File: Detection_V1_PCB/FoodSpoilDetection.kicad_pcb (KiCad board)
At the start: 2 copper layers, 7 parts, among them J1 Conn_01x07_Pin, J2 Conn_01x07_Pin, J3 Conn_01x03_Pin, J4 Conn_01x03_Pin, J5 Conn_01x03_Pin, J6 Conn_01x10_Pin, Q1 Q_NMOS_GSD

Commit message: pcb edits
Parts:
- added J7: Conn_01x04_Pin, Connector_PinHeader_2.54mm:PinHeader_1x04_P2.54mm_Vertical, F.Cu at (218.2, 47.0)
- added Q2: Q_NMOS_GSD, BSS138:SOT-23_3L_ONS, F.Cu at (124.0, 84.0)
- added R1: 10k, Resistor_SMD:R_0603_1608Metric_Pad0.98x0.95mm_HandSolder, F.Cu at (131.5, 88.5)
- added R2: 10k, Resistor_SMD:R_0603_1608Metric_Pad0.98x0.95mm_HandSolder, F.Cu at (124.0, 88.5)
- added R3: 10k, Resistor_SMD:R_0603_1608Metric_Pad0.98x0.95mm_HandSolder, F.Cu at (124.1, 79.0)
- added R4: 10k, Resistor_SMD:R_0603_1608Metric_Pad0.98x0.95mm_HandSolder, F.Cu at (131.5, 79.0)
- moved J2 57.4 mm to (116.4, 30.5), turned to 90 degrees
- moved J1 45.7 mm to (131.6, 40.5), turned to -90 degrees
- moved J5 43.1 mm to (190.4, 47.0), turned to 90 degrees
- moved J4 38.8 mm to (174.5, 47.0), turned to 90 degrees
- moved J6 25.6 mm to (164.4, 67.5), turned to -90 degrees
- moved J3 21.7 mm to (158.4, 47.5), turned to 90 degrees
- moved Q1 8.23 mm to (131.5, 84.0), turned to 180 degrees
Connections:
- J3 pad 3: /Vout -> /5V-A0
- J4 pad 3: /Vout -> /5V-A1
- J5 pad 3: /Vout -> /5V-A2
- Q1 pad 1: unconnected-(Q1-G-Pad1) -> /3V3
- Q1 pad 2: unconnected-(Q1-S-Pad2) -> /SCL-3V
- Q1 pad 3: unconnected-(Q1-D-Pad3) -> /SCL-5V
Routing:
- net /5V: track 0.00 -> 475.4 mm
- net /GND: track 0.00 -> 358.3 mm, vias 0 -> 5
- net /SDA-5V: track 0.00 -> 137.6 mm
- net /SCL-5V: track 0.00 -> 117.7 mm
- net /3V3: track 0.00 -> 114.8 mm
- net /SDA-3V: track 0.00 -> 43.9 mm
- net /SCL-3V: track 0.00 -> 43.1 mm
- net /5V-A2: track 0.00 -> 42.1 mm
- net /5V-A1: track 0.00 -> 28.9 mm
- net /5V-A0: track 0.00 -> 22.8 mm

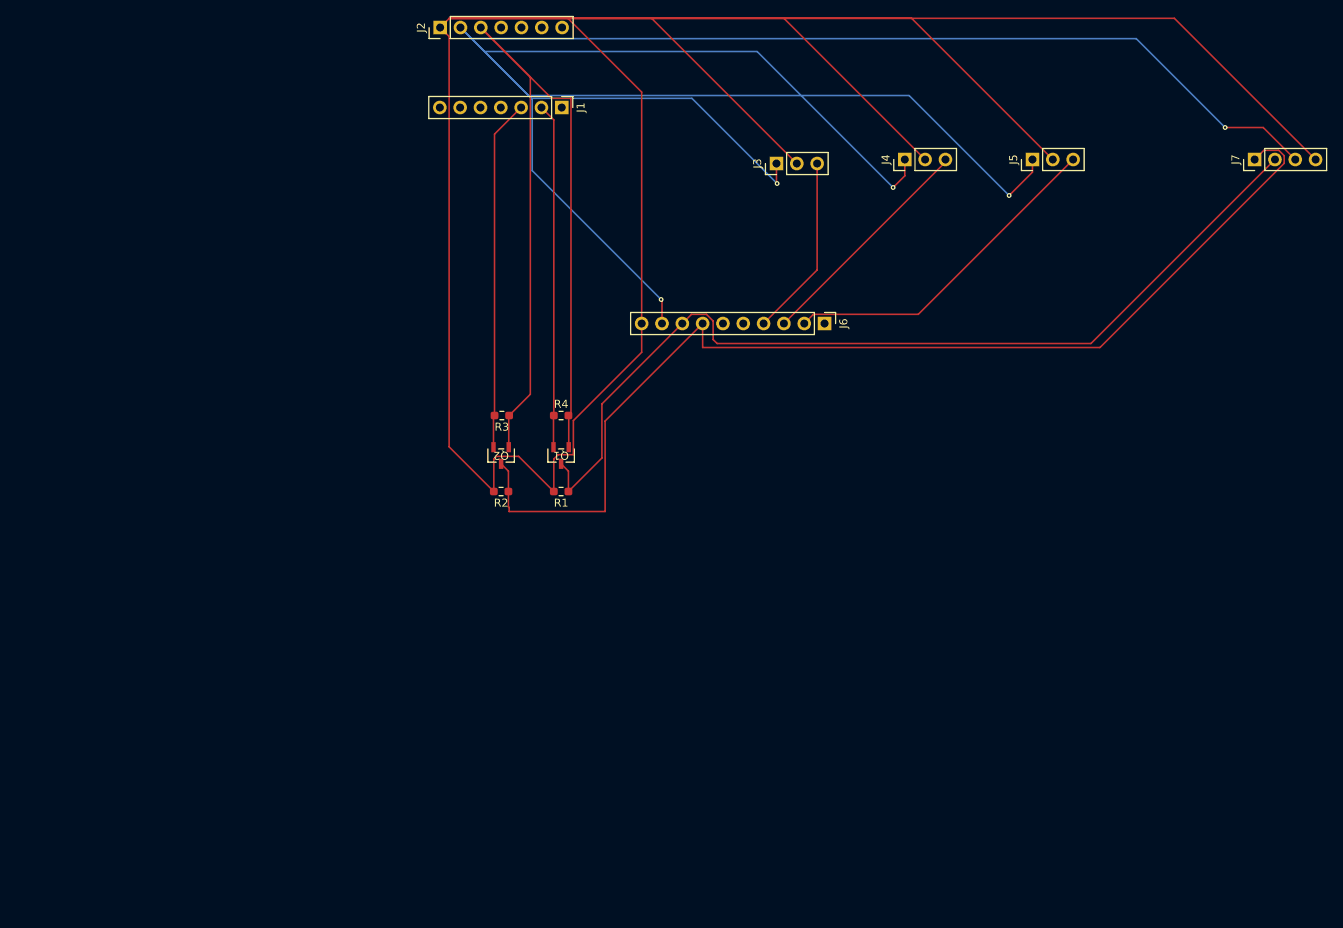
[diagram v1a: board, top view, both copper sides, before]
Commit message: changes to PCB -- Added LEDs and rearranged Layout
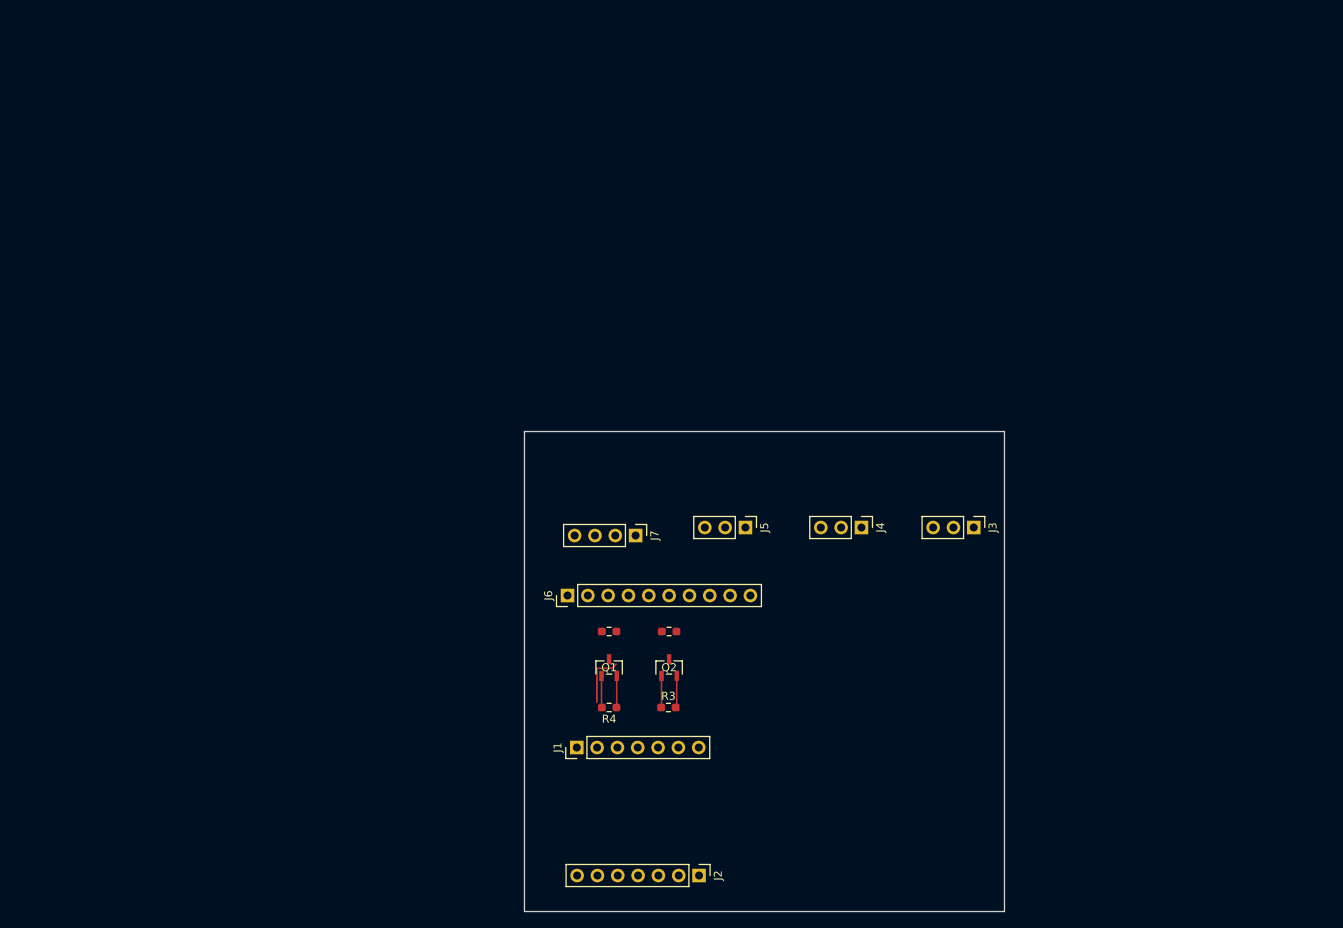
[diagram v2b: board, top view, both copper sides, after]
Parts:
- moved J2 110.8 mm to (148.7, 136.5), turned to -90 degrees
- moved J7 90.5 mm to (140.8, 94.0), turned to -90 degrees
- moved J1 80.0 mm to (133.5, 120.5), turned to 90 degrees
- moved J5 58.3 mm to (154.5, 93.0), turned to -90 degrees
- moved J3 51.8 mm to (183.1, 93.0), turned to -90 degrees
- moved J6 46.8 mm to (132.3, 101.5), turned to 90 degrees
- moved J4 46.3 mm to (169.0, 93.0), turned to -90 degrees
- moved R3 42.0 mm to (144.9, 115.5), turned to 0 degrees
- moved R4 37.0 mm to (137.5, 115.5), turned to 180 degrees
- moved Q2 33.8 mm to (145.0, 110.5), turned to 0 degrees
- moved R2 27.3 mm to (145.0, 106.0), turned to 0 degrees
- moved Q1 27.2 mm to (137.5, 110.5), turned to 0 degrees
- moved R1 18.5 mm to (137.5, 106.0), turned to 0 degrees
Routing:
- net /5V: track 475.4 -> 6.93 mm
- net /GND: track 358.3 -> 0.00 mm, vias 5 -> 0
- net /SDA-5V: track 137.6 -> 0.00 mm
- net /SCL-5V: track 117.7 -> 0.00 mm
- net /3V3: track 114.8 -> 8.40 mm
- net /5V-A2: track 42.1 -> 0.00 mm
- net /SDA-3V: track 43.9 -> 4.01 mm
- net /SCL-3V: track 43.1 -> 3.98 mm
- net /5V-A1: track 28.9 -> 0.00 mm
- net /5V-A0: track 22.8 -> 0.00 mm
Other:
- board outline added: 60 x 60 mm

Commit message: pcb changes
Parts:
- removed R4: 10k, Resistor_SMD:R_0603_1608Metric_Pad0.98x0.95mm_HandSolder
- added D1: LED, LED_SMD:LED_0603_1608Metric_Pad1.05x0.95mm_HandSolder, F.Cu at (87.4, 110.3)
- added D2: LED, LED_SMD:LED_0603_1608Metric_Pad1.05x0.95mm_HandSolder, F.Cu at (87.4, 112.9)
- added D3: LED, LED_SMD:LED_0603_1608Metric_Pad1.05x0.95mm_HandSolder, F.Cu at (87.4, 115.5)
- added D4: LED, LED_SMD:LED_0603_1608Metric_Pad1.05x0.95mm_HandSolder, F.Cu at (87.4, 118.1)
- added D5: LED, LED_SMD:LED_0603_1608Metric_Pad1.05x0.95mm_HandSolder, F.Cu at (87.4, 120.7)
- added D6: LED, LED_SMD:LED_0603_1608Metric_Pad1.05x0.95mm_HandSolder, F.Cu at (87.4, 123.2)
- added D7: LED, LED_SMD:LED_0603_1608Metric_Pad1.05x0.95mm_HandSolder, F.Cu at (87.4, 125.8)
- added D8: LED, LED_SMD:LED_0603_1608Metric_Pad1.05x0.95mm_HandSolder, F.Cu at (87.4, 128.4)
- added Q3: AO3401A, Package_TO_SOT_SMD:SOT-23, F.Cu at (78.1, 90.4)
- Q1: value Q_NMOS_GSD -> AO3400A; footprint BSS138:SOT-23_3L_ONS -> Package_TO_SOT_SMD:SOT-23
- Q2: value Q_NMOS_GSD -> AO3401A; footprint BSS138:SOT-23_3L_ONS -> Package_TO_SOT_SMD:SOT-23
- R1: value 10k -> 10ohm
- R2, R3: value 10k -> 100k
- moved J2 69.2 mm to (80.0, 128.4)
- moved J3 67.3 mm to (116.1, 86.9)
- moved J7 67.3 mm to (73.8, 87.9)
- moved J4 67.3 mm to (102.0, 86.9)
- moved J5 67.3 mm to (87.5, 86.9)
- moved J1 66.8 mm to (68.8, 103.9)
- moved R3 66.6 mm to (83.0, 90.9)
- moved Q2 56.9 mm to (92.4, 88.8)
- moved R2 50.0 mm to (97.0, 91.9)
- moved Q1 45.8 mm to (93.1, 121.4)
- moved R1 44.3 mm to (93.6, 111.9)
- moved J6 26.4 mm to (111.0, 117.0), turned to 180 degrees
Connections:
- J3 pad 2: /5V -> Net-(J3-Pin_2)
- J3 pad 3: /5V-A0 -> /A1
- J4 pad 2: /5V -> Net-(J3-Pin_2)
- J4 pad 3: /5V-A1 -> (no net)
- J5 pad 2: /5V -> Net-(J3-Pin_2)
- J5 pad 3: /5V-A2 -> /A3
- J6 pad 1: /5V-A3 -> /A3
- J6 pad 10: /5V -> /3V3
- J6 pad 2: /5V-A2 -> (no net)
- J6 pad 3: /5V-A1 -> /A1
- J6 pad 4: /5V-A0 -> /A0
- J6 pad 7: /SDA-5V -> /SDA-3V
- J6 pad 8: /SCL-5V -> /SCL-3V
- J7 pad 1: /SDA-5V -> /SDA-3V
- J7 pad 2: /SCL-5V -> /SCL-3V
- J7 pad 4: /5V -> Net-(J7-Pin_4)
- Q1 pad 1: /3V3 -> /D7
- Q1 pad 2: /SCL-3V -> /GND
- Q1 pad 3: /SCL-5V -> Net-(D1-K)
- Q2 pad 1: /3V3 -> /D9
- Q2 pad 2: /SDA-3V -> /GND
- Q2 pad 3: /SDA-5V -> Net-(J3-Pin_2)
- R1 pad 1: /SCL-5V -> /3V3
- R1 pad 2: /5V -> Net-(D1-A)
- R2 pad 1: /SDA-5V -> /3V3
- R2 pad 2: /5V -> /D9
- R3 pad 2: /SDA-3V -> /D10
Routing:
- net Net-(D1-A): track 0.00 -> 31.1 mm
- net /3V3: track 8.40 -> 0.00 mm
- net /5V: track 6.93 -> 0.00 mm
- net /SDA-3V: track 4.01 -> 0.00 mm
- net /SCL-3V: track 3.98 -> 0.00 mm

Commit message: updated schematic (almost finalized)
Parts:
- removed J1, J2: Conn_01x07_Pin, Connector_PinHeader_2.54mm:PinHeader_1x07_P2.54mm_Vertical
- added J9: Conn_01x10_Socket, Connector_PinSocket_2.54mm:PinSocket_1x10_P2.54mm_Vertical, F.Cu at (167.3, 134.6)
- added R10: 100K, Resistor_SMD:R_0603_1608Metric_Pad0.98x0.95mm_HandSolder, F.Cu at (103.6, 114.8)
- added R11: 100K, Resistor_SMD:R_0603_1608Metric_Pad0.98x0.95mm_HandSolder, F.Cu at (103.6, 117.3)
- added R4: 1K, Resistor_SMD:R_0603_1608Metric_Pad0.98x0.95mm_HandSolder, F.Cu at (99.2, 114.8)
- added R5: 1K, Resistor_SMD:R_0603_1608Metric_Pad0.98x0.95mm_HandSolder, F.Cu at (99.2, 117.3)
- added R6: 1K, Resistor_SMD:R_0603_1608Metric_Pad0.98x0.95mm_HandSolder, F.Cu at (99.2, 119.9)
- added R7: 1K, Resistor_SMD:R_0603_1608Metric_Pad0.98x0.95mm_HandSolder, F.Cu at (103.6, 107.3)
- added R8: 1K, Resistor_SMD:R_0603_1608Metric_Pad0.98x0.95mm_HandSolder, F.Cu at (103.6, 109.8)
- added R9: 100K, Resistor_SMD:R_0603_1608Metric_Pad0.98x0.95mm_HandSolder, F.Cu at (103.6, 112.3)
- added U1: XIAO-ESP32-S3-DIP, esp32s3:XIAO-ESP32-S3-DIP, F.Cu at (155.4, 107.4)
- D1, D2, D3, D4, D5, D6, D7, D8: footprint LED_SMD:LED_0603_1608Metric_Pad1.05x0.95mm_HandSolder -> LED_SMD:LED_0603_1608Metric
- J3, J4: value Conn_01x03_Pin -> Conn_01x03_Socket; footprint Connector_PinHeader_2.54mm:PinHeader_1x03_P2.54mm_Vertical -> Connector_PinSocket_2.54mm:PinSocket_1x03_P2.54mm_Vertical
- J5: value Conn_01x03_Pin -> Conn_01x04_Socket; footprint Connector_PinHeader_2.54mm:PinHeader_1x03_P2.54mm_Vertical -> Connector_PinSocket_2.54mm:PinSocket_1x04_P2.54mm_Vertical
- J6: value Conn_01x10_Pin -> Conn_01x03_Socket; footprint Connector_PinHeader_2.54mm:PinHeader_1x10_P2.54mm_Vertical -> Connector_PinSocket_2.54mm:PinSocket_1x03_P2.54mm_Vertical
- J7: value Conn_01x04_Pin -> Conn_01x06_Socket; footprint Connector_PinHeader_2.54mm:PinHeader_1x04_P2.54mm_Vertical -> Connector_PinSocket_2.54mm:PinSocket_1x06_P2.54mm_Vertical
- R1: value 10ohm -> 1K
- R2, R3: value 100k -> 1K
- moved D2 87.7 mm to (173.0, 94.0)
- moved D7 86.9 mm to (172.2, 107.2)
- moved D5 85.2 mm to (172.6, 119.6)
- moved D1 71.1 mm to (156.2, 92.6)
- moved D8 69.0 mm to (155.8, 119.8)
- moved Q3 68.4 mm to (130.1, 134.8)
- moved J7 62.2 mm to (135.8, 93.3), turned to 0 degrees
- moved J3 58.2 mm to (174.2, 83.4)
- moved D3 57.3 mm to (140.2, 93.2)
- moved J6 56.8 mm to (156.8, 83.4), turned to -90 degrees
- moved Q2 53.5 mm to (130.1, 126.8)
- moved D4 53.1 mm to (139.6, 108.6)
- moved D6 52.7 mm to (140.0, 120.0)
- moved J5 40.7 mm to (127.2, 96.0), turned to 0 degrees
- moved Q1 36.5 mm to (129.5, 118.4)
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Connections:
- D2 pad 2: Net-(D1-A) -> Net-(D2-A)
- D3 pad 2: Net-(D1-A) -> Net-(D3-A)
- D4 pad 2: Net-(D1-A) -> Net-(D4-A)
- D5 pad 2: Net-(D1-A) -> Net-(D5-A)
- D6 pad 2: Net-(D1-A) -> Net-(D6-A)
- D7 pad 2: Net-(D1-A) -> Net-(D7-A)
- D8 pad 2: Net-(D1-A) -> Net-(D8-A)
- J3 pad 1: /GND -> /A1
- J3 pad 3: /A1 -> GND
- J4 pad 1: /GND -> /A2
- J4 pad 3: (no net) -> GND
- J5 pad 1: /GND -> Net-(J5-Pin_1)
- J5 pad 2: Net-(J3-Pin_2) -> GND
- J5 pad 3: /A3 -> SCL
- J6 pad 2: (no net) -> Net-(J3-Pin_2)
- J6 pad 3: /A1 -> GND
- J7 pad 1: /SDA-3V -> unconnected-(J7-Pin_1-Pad1)
- J7 pad 2: /SCL-3V -> unconnected-(J7-Pin_2-Pad2)
- J7 pad 3: /GND -> unconnected-(J7-Pin_3-Pad3)
- J7 pad 4: Net-(J7-Pin_4) -> unconnected-(J7-Pin_4-Pad4)
- Q1 pad 1: /D7 -> Net-(Q1-G)
- Q1 pad 2: /GND -> GND
- Q2 pad 1: /D9 -> D1
- Q2 pad 2: /GND -> GND
- Q3 pad 1: /D10 -> D0
- Q3 pad 2: /GND -> GND
- Q3 pad 3: Net-(J7-Pin_4) -> Net-(J5-Pin_1)
- R1 pad 1: /3V3 -> Net-(D2-A)
- R1 pad 2: Net-(D1-A) -> 3v3
- R2 pad 1: /3V3 -> Net-(D1-A)
- R2 pad 2: /D9 -> 3v3
- R3 pad 1: /3V3 -> Net-(D3-A)
- R3 pad 2: /D10 -> 3v3
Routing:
- net Net-(D1-A): track 31.1 -> 0.00 mm

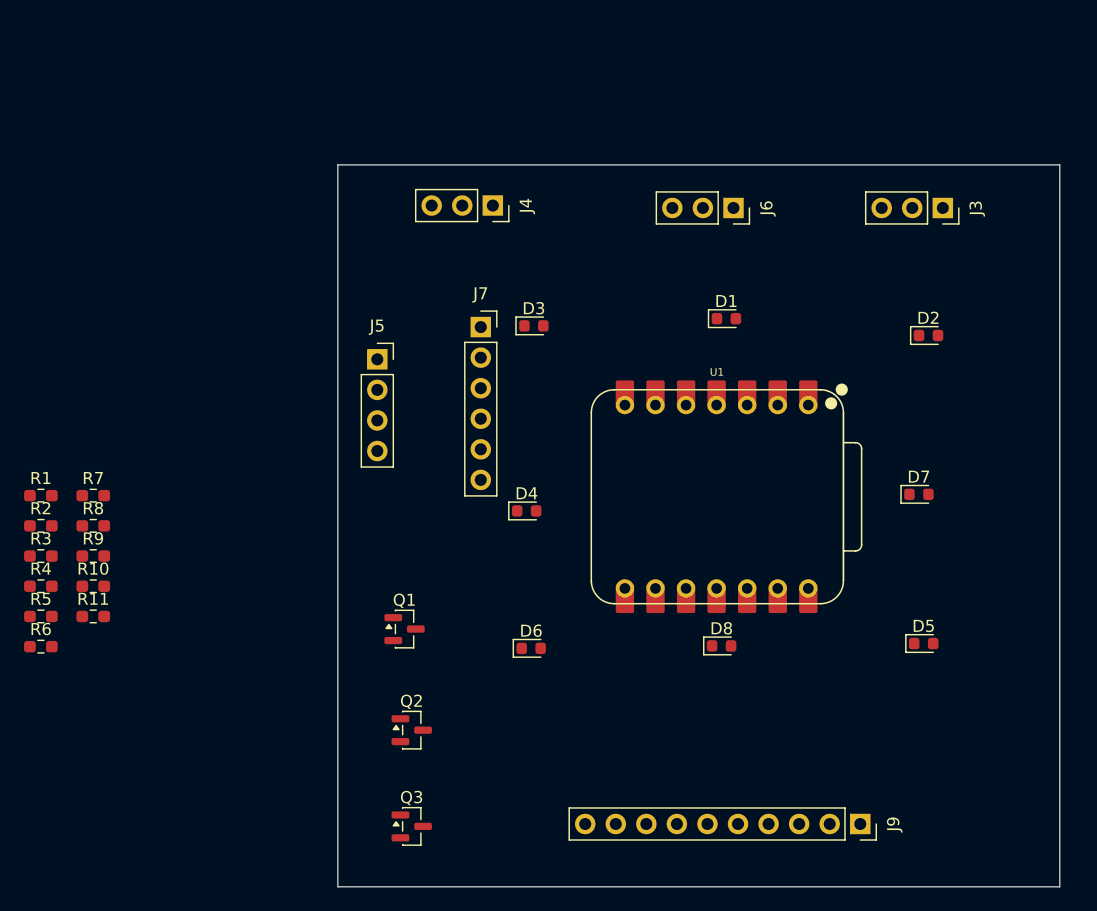
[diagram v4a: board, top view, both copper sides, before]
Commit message: added mounting holes
Need to align mounting holes and fiduciaries
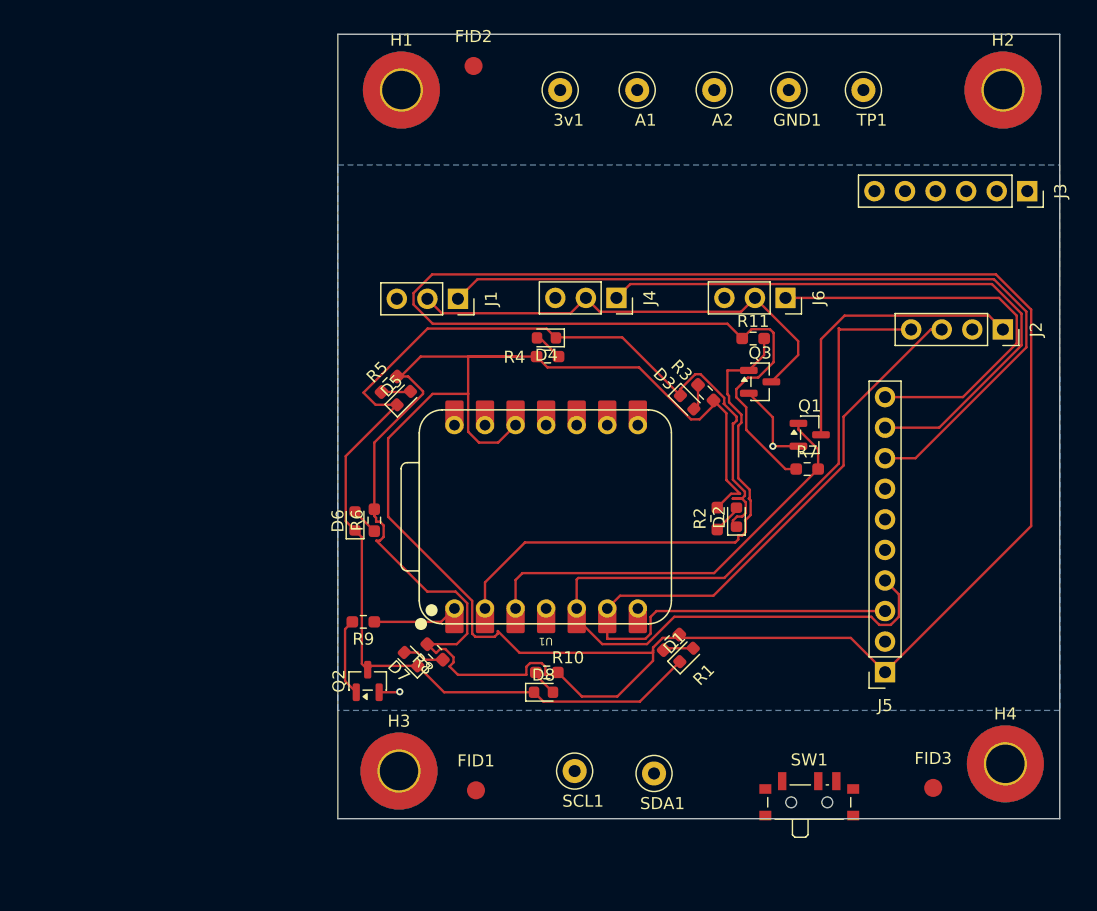
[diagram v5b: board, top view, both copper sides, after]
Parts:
- added 3v1: TestPoint, TestPoint:TestPoint_Loop_D1.80mm_Drill1.0mm_Beaded, F.Cu at (142.4, 73.6)
- added A1: TestPoint, TestPoint:TestPoint_Loop_D1.80mm_Drill1.0mm_Beaded, F.Cu at (148.8, 73.6)
- added A2: TestPoint, TestPoint:TestPoint_Loop_D1.80mm_Drill1.0mm_Beaded, F.Cu at (155.2, 73.6)
- added FID1: Fiducial, Fiducial:Fiducial_1.5mm_Mask3mm, F.Cu at (135.4, 131.8)
- added FID2: Fiducial, Fiducial:Fiducial_1.5mm_Mask3mm, F.Cu at (135.2, 71.6)
- added FID3: Fiducial, Fiducial:Fiducial_1.5mm_Mask3mm, F.Cu at (173.4, 131.6)
- added GND1: TestPoint, TestPoint:TestPoint_Loop_D1.80mm_Drill1.0mm_Beaded, F.Cu at (161.4, 73.6)
- added H1: MountingHole_Pad, MountingHole:MountingHole_3.2mm_M3_Pad_TopBottom, F.Cu at (129.2, 73.6)
- added H2: MountingHole_Pad, MountingHole:MountingHole_3.2mm_M3_Pad_TopBottom, F.Cu at (179.2, 73.6)
- added H3: MountingHole_Pad, MountingHole:MountingHole_3.2mm_M3_Pad_TopBottom, F.Cu at (129.0, 130.2)
- added H4: MountingHole_Pad, MountingHole:MountingHole_3.2mm_M3_Pad_TopBottom, F.Cu at (179.4, 129.6)
- added SCL1: TestPoint, TestPoint:TestPoint_Loop_D1.80mm_Drill1.0mm_Beaded, F.Cu at (143.6, 130.2)
- added SDA1: TestPoint, TestPoint:TestPoint_Loop_D1.80mm_Drill1.0mm_Beaded, F.Cu at (150.2, 130.4)
- added SW1: SW_DIP_x01, Button_Switch_SMD:SW_SPDT_PCM12, F.Cu at (163.1, 132.5)
- added TP1: A3, TestPoint:TestPoint_Loop_D1.80mm_Drill1.0mm_Beaded, F.Cu at (167.6, 73.6)
- moved R7 60.6 mm to (162.9, 105.1)
- moved R11 58.6 mm to (158.4, 94.2)
- moved R3 56.9 mm to (154.5, 98.8), turned to -45 degrees
- moved R2 56.2 mm to (155.4, 109.2), turned to 90 degrees
- moved R1 53.3 mm to (151.7, 119.5), turned to 45 degrees
- moved J2 52.0 mm to (179.2, 93.5), turned to -90 degrees
- moved D5 47.8 mm to (129.4, 99.2), turned to 45 degrees
- moved J3 46.8 mm to (181.2, 82.0), turned to -90 degrees
- moved Q1 46.4 mm to (163.1, 102.2)
- moved R4 46.2 mm to (141.3, 95.8), turned to 180 degrees
- moved D7 44.4 mm to (130.0, 120.9), turned to 135 degrees
- moved J1 41.0 mm to (133.9, 91.0)
- moved Q3 40.9 mm to (159.0, 97.8)
- moved R10 39.6 mm to (141.3, 122.0)
- moved R5 34.8 mm to (128.2, 98.0), turned to 45 degrees
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- renumbered J3 to J1, J5 to J2, J7 to J3, J9 to J5, Q3 to Q1, Q1 to Q2, Q2 to Q3, R2 to R1, R8 to R10, R10 to R11, R1 to R2, R11 to R7, R7 to R8
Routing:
- net 3v3: track 0.00 -> 316.7 mm
- net Net-(D1-K): track 0.00 -> 107.6 mm
- net SDA: track 0.00 -> 78.1 mm
- net /A1: track 0.00 -> 67.6 mm
- net SCL: track 0.00 -> 66.3 mm
- net /A2: track 0.00 -> 52.0 mm
- net D1: track 0.00 -> 45.5 mm
- net Net-(J1-Pin_2): track 0.00 -> 38.6 mm
- net D2: track 0.00 -> 35.8 mm
- net /A3: track 0.00 -> 34.9 mm
- net Net-(J2-Pin_1): track 0.00 -> 24.3 mm
- net GND: track 0.00 -> 9.31 mm, vias 0 -> 2
- net D0: track 0.00 -> 7.12 mm
- net Net-(Q2-G): track 0.00 -> 6.48 mm
- net Net-(D7-A): track 0.00 -> 3.45 mm
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- added copper zone on B.Cu, net GND
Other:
- board size 60 x 60 mm -> 60 x 65.2 mm
